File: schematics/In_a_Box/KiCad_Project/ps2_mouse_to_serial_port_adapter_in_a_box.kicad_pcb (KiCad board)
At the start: 2 copper layers, 91.4 x 71.1 mm, 28 parts, among them J1 DC IN, J2 PS/2 & USB, J3 Serial Port, Q1 BC547, SW1 Switch ON/OFF, U1 74LS00, U2 L78L05, U3 L7805

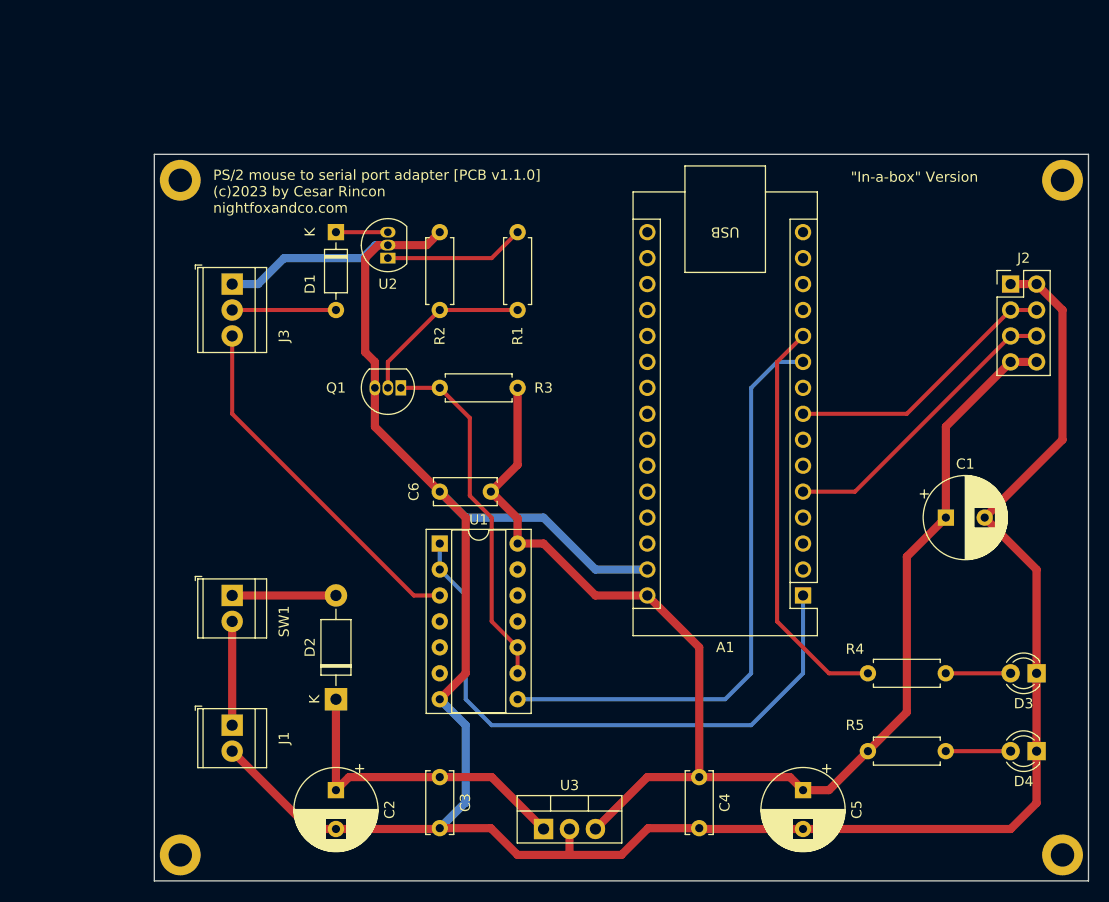
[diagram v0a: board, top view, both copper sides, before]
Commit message: v1.5.0
- Ajustadas las placas "Stand alone" y "In-a-box" al tamaño standard de
  90x70 mm.
- Añadidas a estas placas las zonas de relleno a masa (GND).
- Añadidas las serigrafias con los valores de todos los componentes en todas
  las versiones de las placas.
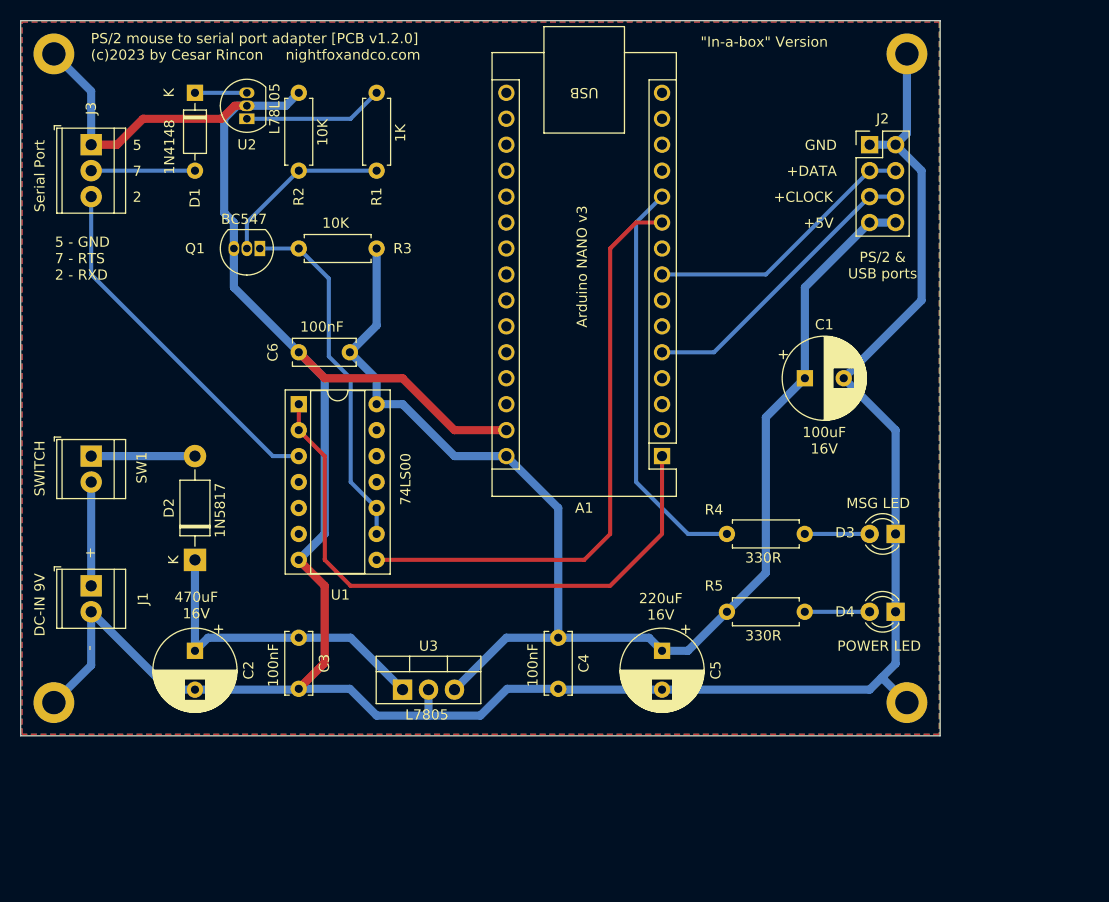
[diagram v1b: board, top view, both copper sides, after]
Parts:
- moved ? 19.4 mm to (100.5, 80.3)
- moved ? 19.4 mm to (14.1, 80.3)
- moved C3 19.4 mm to (39.5, 72.7)
- moved C4 19.4 mm to (64.9, 72.7)
- moved C5 19.4 mm to (75.1, 74.0)
- moved D3 19.4 mm to (98.0, 62.6)
- moved J1 19.4 mm to (19.2, 67.6)
- moved R4 19.4 mm to (81.4, 62.6)
- moved ? 19.4 mm to (100.5, 14.3)
- moved C2 19.4 mm to (29.4, 74.0)
- moved D1 19.4 mm to (29.4, 19.4)
- moved J2 19.4 mm to (95.4, 24.5)
- moved J3 19.4 mm to (19.2, 24.5)
- moved R1 19.4 mm to (47.2, 27.0)
- moved R2 19.4 mm to (39.5, 27.0)
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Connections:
- net Net-(A1-VIN) renamed /+5V
- ? pad GND: (no net) -> /GND (x4)
- A1 pad 29: Net-(D3-K) -> /GND
- C1 pad 2: Net-(D3-K) -> /GND
- C2 pad 2: Net-(D3-K) -> /GND
- C3 pad 2: Net-(D3-K) -> /GND
- C4 pad 2: Net-(D3-K) -> /GND
- C5 pad 2: Net-(D3-K) -> /GND
- C6 pad 2: Net-(D3-K) -> /GND
- D3 pad 1: Net-(D3-K) -> /GND
- D4 pad 1: Net-(D3-K) -> /GND
- J1 pad 2: Net-(D3-K) -> /GND
- J2 pad 1: Net-(D3-K) -> /GND
- J2 pad 2: Net-(D3-K) -> /GND
- J3 pad 1: Net-(D3-K) -> /GND
- Q1 pad 3: Net-(D3-K) -> /GND
- R2 pad 2: Net-(D3-K) -> /GND
- U1 pad 7: Net-(D3-K) -> /GND
- U2 pad 2: Net-(D3-K) -> /GND
- U3 pad 2: Net-(D3-K) -> /GND
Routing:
- net /GND: track 0.00 -> 292.5 mm
- net Net-(D3-K): track 258.9 -> 0.00 mm
- added copper zone on B.Cu, net /GND
- added copper zone on F.Cu, net /GND
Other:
- board size 91.4 x 71.1 mm -> 90 x 70 mm
- board text added: "+"
- board text added: "+5V"
- board text added: "+CLOCK"
- board text added: "+DATA"
- board text added: "-"
- board text added: "100nF"
- board text added: "100uF 16V"
- board text added: "10K"
- board text added: "1K"
- board text added: "1N4148"
- board text added: "1N5817"
- board text added: "2"
- board text added: "220uF 16V"
- board text added: "330R"
- board text added: "470uF 16V"
- board text added: "5"
- board text added: "5 - GND 7 - RTS 2 - RXD"
- board text added: "7"
- board text added: "74LS00"
- board text added: "Arduino NANO v3"
- board text added: "BC547"
- board text added: "DC-IN 9V"
- board text added: "GND"
- board text added: "L7805"
- board text added: "L78L05"
- board text added: "MSG LED"
- board text added: "POWER LED"
- board text added: "PS/2 & USB ports"
- board text added: "PS/2 mouse to serial port adapter [PCB v1.2.0] (c)2023 by Cesar Rincon nightfoxandco.com"
- board text added: "SWITCH"
- board text added: "Serial Port"
- board text removed: "PS/2 mouse to serial port adapter [PCB v1.1.0] (c)2023 by Cesar Rincon nightfoxandco.com"

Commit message: v1.5.1
- Arreglada la serigrafía del conector MINI-DIN-6 (PS/2), la cual se superponía en algunas zonas de soldado.
- En todas las placas se añade el símbolo de los agujeros de montaje con el tamaño estándar M3.
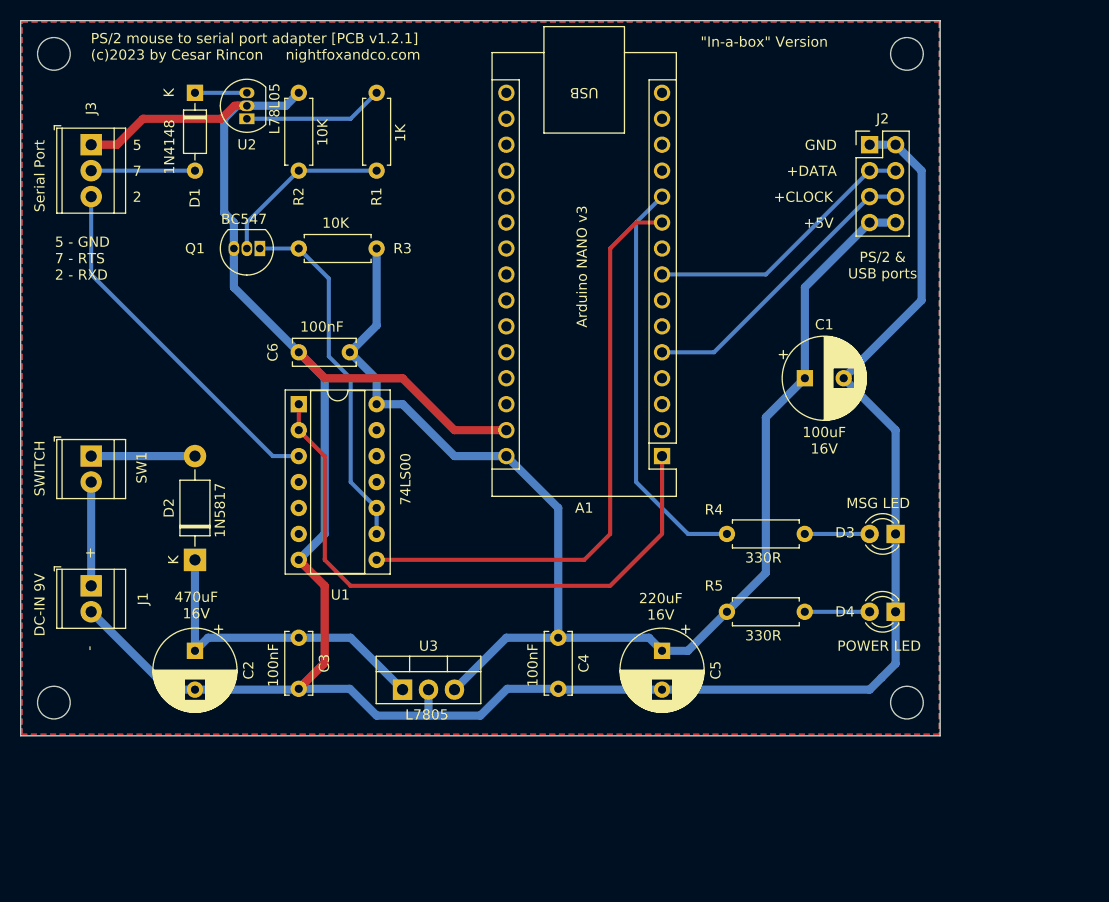
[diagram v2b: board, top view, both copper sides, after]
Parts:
- removed ? (x4): , 
- added H1: MountingHole, MountingHole:MountingHole_3.2mm_M3, F.Cu at (15.6, 15.6)
- added H2: MountingHole, MountingHole:MountingHole_3.2mm_M3, F.Cu at (99.1, 15.6)
- added H3: MountingHole, MountingHole:MountingHole_3.2mm_M3, F.Cu at (15.6, 79.1)
- added H4: MountingHole, MountingHole:MountingHole_3.2mm_M3, F.Cu at (99.1, 79.1)
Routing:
- net /GND: track 292.5 -> 258.9 mm
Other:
- board text added: "PS/2 mouse to serial port adapter [PCB v1.2.1] (c)2023 by Cesar Rincon nightfoxandco.com"
- board text removed: "PS/2 mouse to serial port adapter [PCB v1.2.0] (c)2023 by Cesar Rincon nightfoxandco.com"

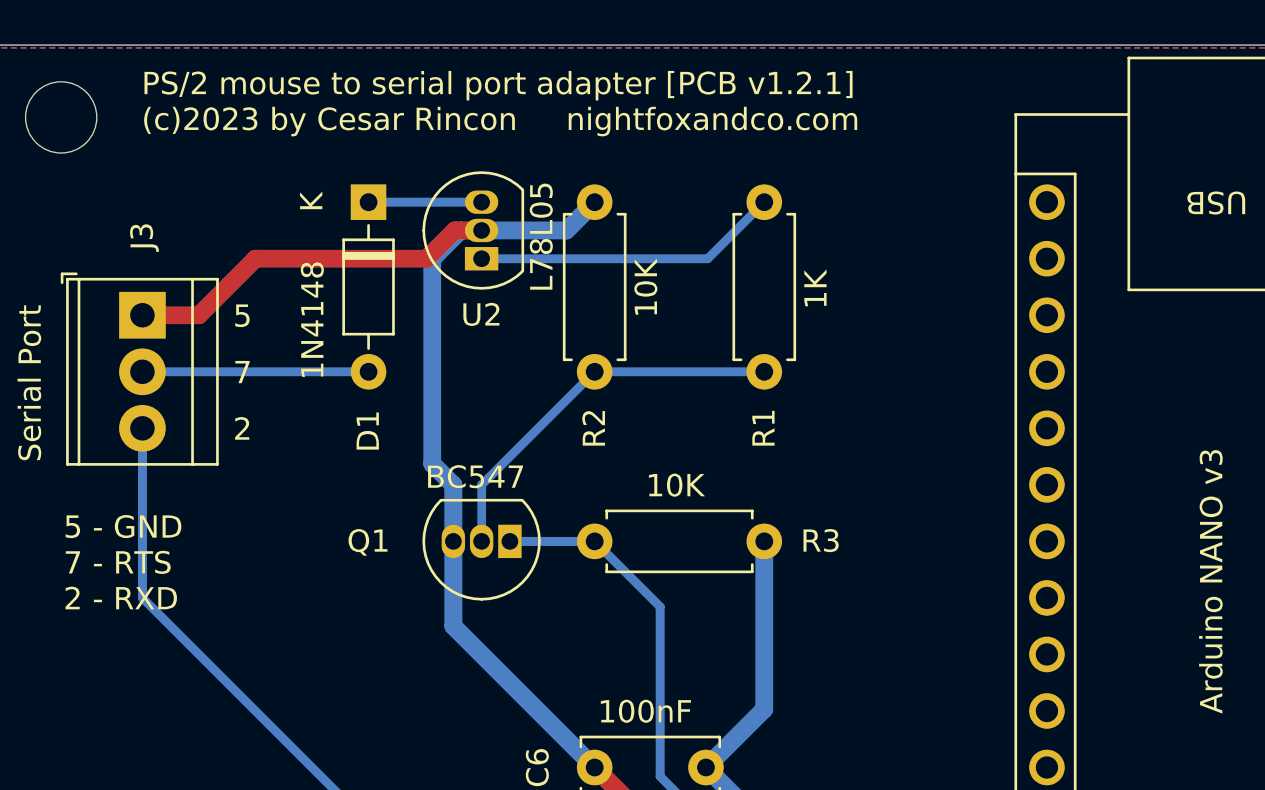
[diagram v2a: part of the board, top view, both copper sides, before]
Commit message: v1.7.0
- Modificadas las huellas de todas las placas para que los componentes TO92 resulten más fáciles de soldar a mano.
- Modificadas las conexiones del conector IDC en la placa ISA para poder usar un cable IDC a DB9 comercial, sin necesidad de realizarle modificaciones.
- Añadido el modelo en formato FreeCad y el archivo STL del soporte para la placa ISA. Estos archivos estan preparados para poder realizar la impresión en 3D del soporte. Se recomienda un in-fill del 100%.
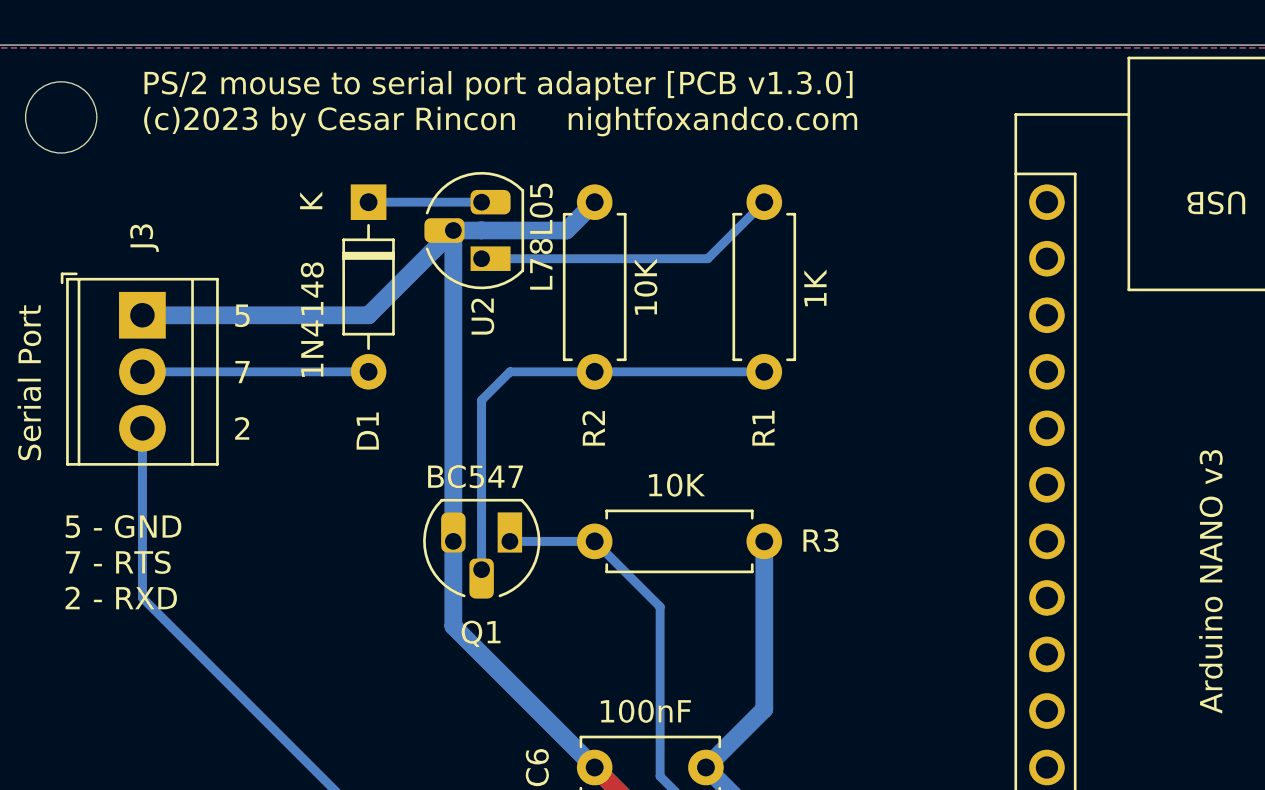
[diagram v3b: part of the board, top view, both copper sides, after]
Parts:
- Q1, U2: footprint Package_TO_SOT_THT:TO-92_Inline -> Package_TO_SOT_THT:TO-92_HandSolder
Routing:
- net Net-(Q1-B): track 17.3 -> 20.8 mm
- net /GND: track 258.9 -> 256.7 mm
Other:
- board text added: "PS/2 mouse to serial port adapter [PCB v1.3.0] (c)2023 by Cesar Rincon nightfoxandco.com"
- board text removed: "PS/2 mouse to serial port adapter [PCB v1.2.1] (c)2023 by Cesar Rincon nightfoxandco.com"
